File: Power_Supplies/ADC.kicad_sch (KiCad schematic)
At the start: 0 parts

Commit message: Added ADC schematic
yes
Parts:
- added C36, C38, C40: 0.1uF, Capacitor_SMD:C_0805_2012Metric, symbol Device:C
- added C37, C39, C41: 10uF, Capacitor_SMD:CP_Elec_4x5.8, symbol Device:C_Polarized_US
- added C42, C43: 1uF, Capacitor_SMD:CP_Elec_4x5.8, symbol Device:C_Polarized_US
- added IC1: PCM1808PWRG4, SamacSys_Parts:SOP65P640X120-14N, symbol SamacSys_Parts:PCM1808PWRG4
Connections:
- new net: C43.1, IC1.13 (VINL)
- new net: C42.1, IC1.14 (VINR)
- new net: C40.1, C41.1, IC1.1 (VREF)
- new net 3.3V: C38.2, C39.1, IC1.4 (VDD)
- new net 5V: C36.1, C37.1, IC1.3 (VCC)
- new net AGND: C36.2, C37.2, C38.1, C39.2, C40.2, C41.2, IC1.2 (AGND), IC1.5 (DGND)
- new net A_L_1: C43.2
- new net A_R_1: C42.2
- new net DATA_BIT_CLOCK: IC1.8 (BCK)
- new net D_OUT_1: IC1.9 (DOUT)
- new net FORMAT_SELECT: IC1.12 (FMT)
- new net LRCK: IC1.7 (LRCK)
- new net MCLK: IC1.6 (SCKI)
- new net MODE_0: IC1.10 (MD0)
- new net MODE_1: IC1.11 (MD1)

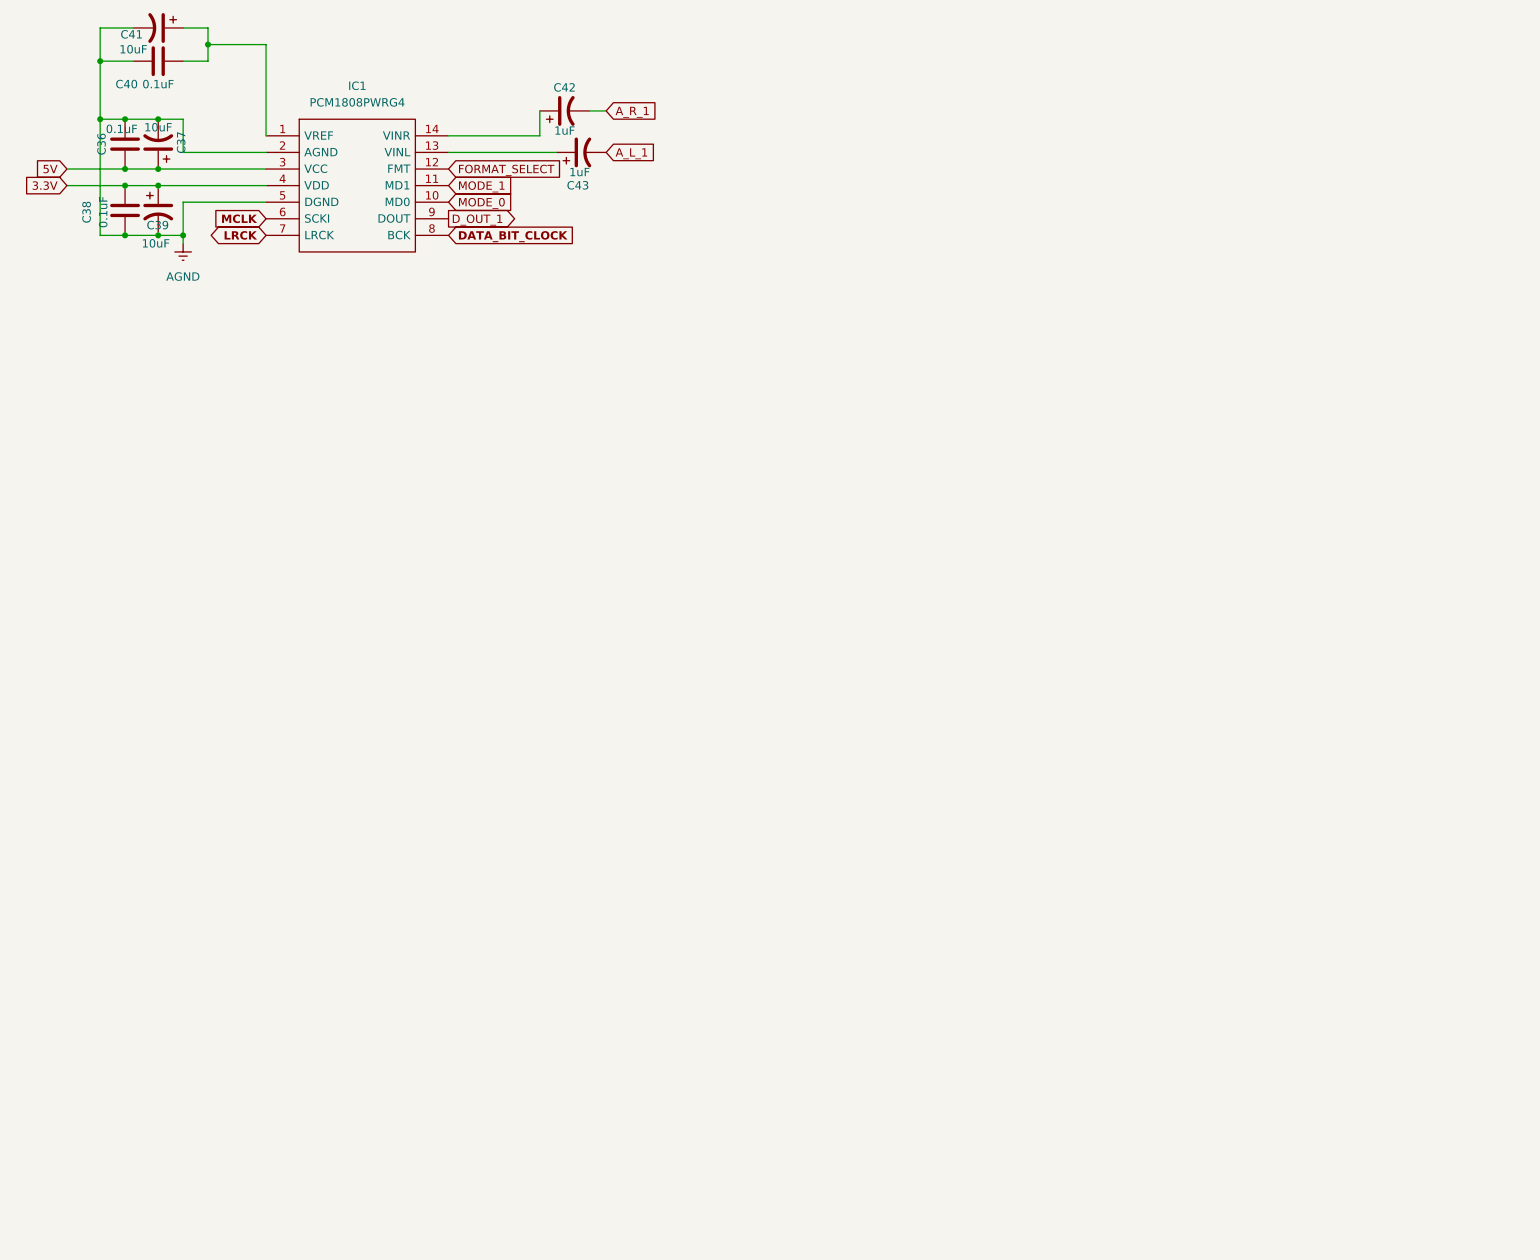
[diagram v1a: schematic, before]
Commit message: Added Phantom Power, updated Xcore library things
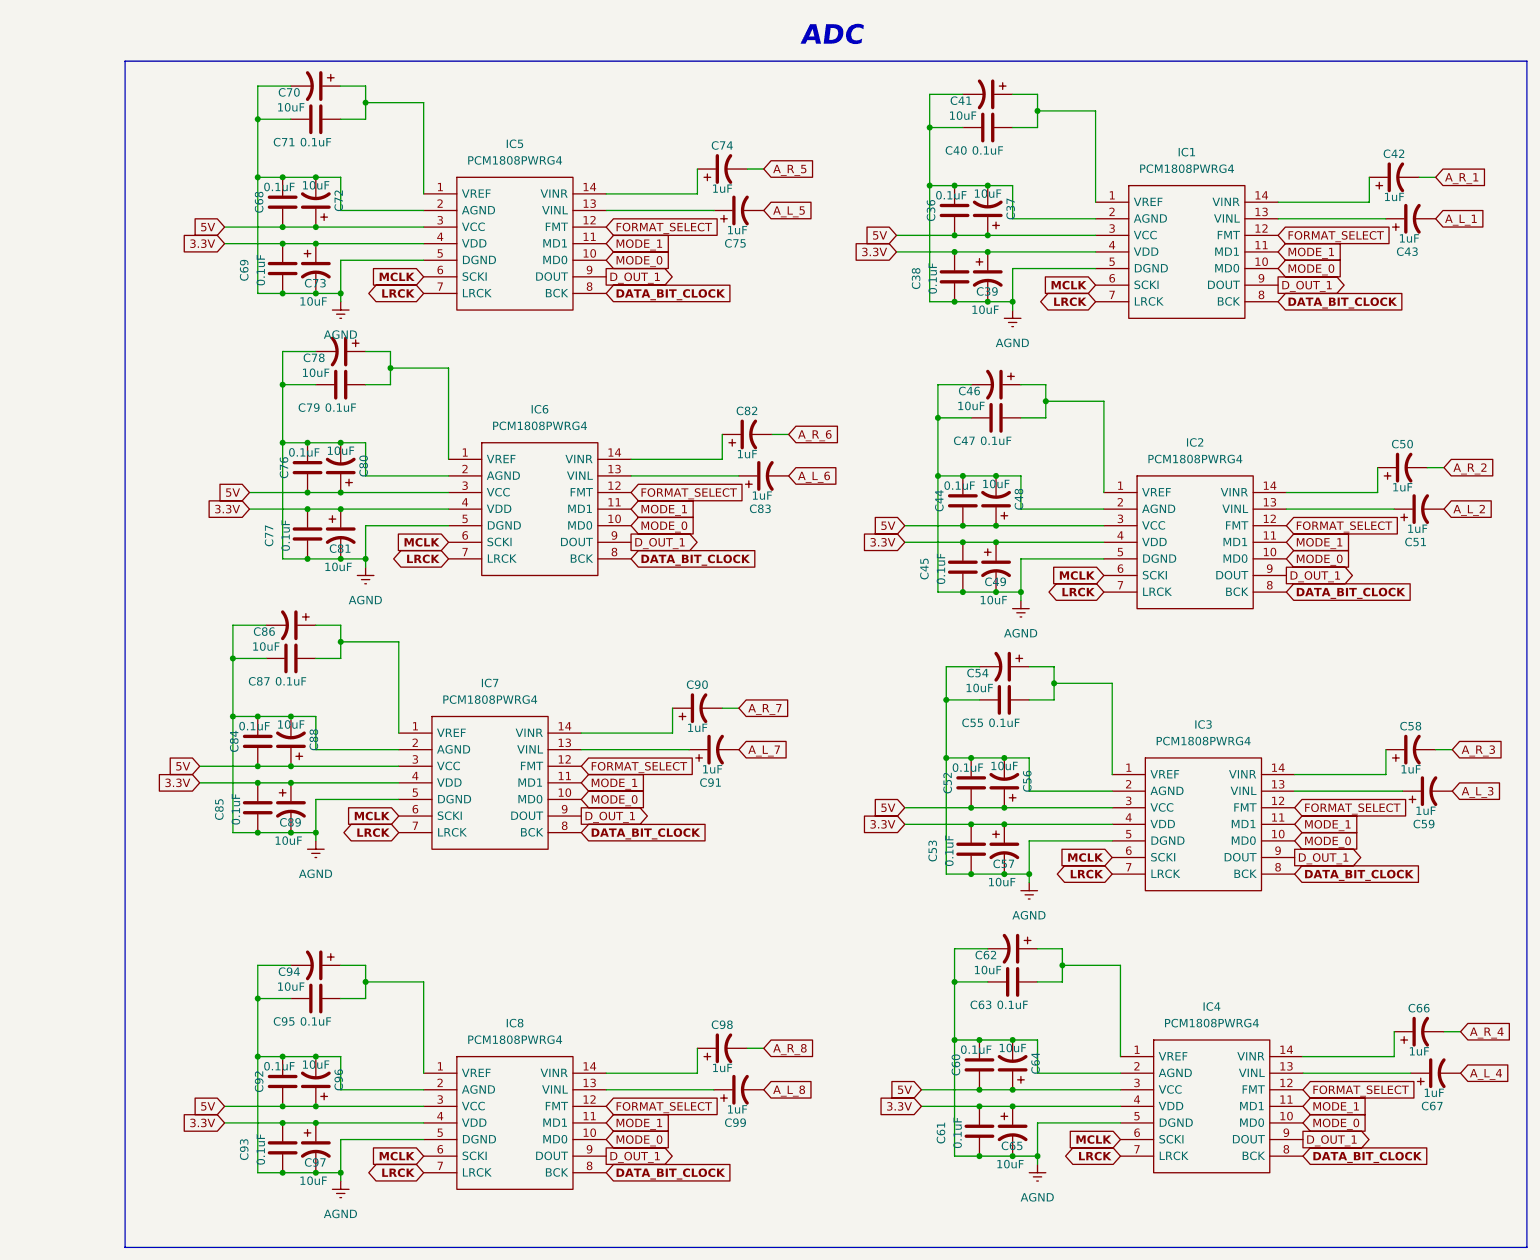
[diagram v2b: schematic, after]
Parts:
- added C44, C45, C47, C52, C53, C55, C60, C61, C63, C68, C69, C71, C76, C77, C79, C84, C85, C87, C92, C93, C95: 0.1uF, Capacitor_SMD:C_0805_2012Metric, symbol Device:C
- added C46, C48, C49, C54, C56, C57, C62, C64, C65, C70, C72, C73, C78, C80, C81, C86, C88, C89, C94, C96, C97: 10uF, Capacitor_SMD:CP_Elec_4x5.8, symbol Device:C_Polarized_US
- added C50, C51, C58, C59, C66, C67, C74, C75, C82, C83, C90, C91, C98, C99: 1uF, Capacitor_SMD:CP_Elec_4x5.8, symbol Device:C_Polarized_US
- added IC2, IC3, IC4, IC5, IC6, IC7, IC8: PCM1808PWRG4, SamacSys_Parts:SOP65P640X120-14N, symbol SamacSys_Parts:PCM1808PWRG4
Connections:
- net 3.3V: now also C45.2, C49.1, C53.2, C57.1, C61.2, C65.1, C69.2, C73.1, C77.2, C81.1, C85.2, C89.1, C93.2, C97.1, IC2.4 (VDD), IC3.4 (VDD), IC4.4 (VDD), IC5.4 (VDD), IC6.4 (VDD), IC7.4 (VDD), IC8.4 (VDD)
- net 5V: now also C44.1, C48.1, C52.1, C56.1, C60.1, C64.1, C68.1, C72.1, C76.1, C80.1, C84.1, C88.1, C92.1, C96.1, IC2.3 (VCC), IC3.3 (VCC), IC4.3 (VCC), IC5.3 (VCC), IC6.3 (VCC), IC7.3 (VCC), IC8.3 (VCC)
- net AGND: now also C44.2, C45.1, C46.2, C47.2, C48.2, C49.2, C52.2, C53.1, C54.2, C55.2, C56.2, C57.2, C60.2, C61.1, C62.2, C63.2, C64.2, C65.2, C68.2, C69.1, C70.2, C71.2, C72.2, C73.2, C76.2, C77.1, C78.2, C79.2, C80.2, C81.2, C84.2, C85.1, C86.2, C87.2, C88.2, C89.2, C92.2, C93.1, C94.2, C95.2, C96.2, C97.2, IC2.2 (AGND), IC2.5 (DGND), IC3.2 (AGND), IC3.5 (DGND), IC4.2 (AGND), IC4.5 (DGND), IC5.2 (AGND), IC5.5 (DGND), IC6.2 (AGND), IC6.5 (DGND), IC7.2 (AGND), IC7.5 (DGND), IC8.2 (AGND), IC8.5 (DGND)
- net DATA_BIT_CLOCK: now also IC2.8 (BCK), IC3.8 (BCK), IC4.8 (BCK), IC5.8 (BCK), IC6.8 (BCK), IC7.8 (BCK), IC8.8 (BCK)
- net D_OUT_1: now also IC2.9 (DOUT), IC3.9 (DOUT), IC4.9 (DOUT), IC5.9 (DOUT), IC6.9 (DOUT), IC7.9 (DOUT), IC8.9 (DOUT)
- net FORMAT_SELECT: now also IC2.12 (FMT), IC3.12 (FMT), IC4.12 (FMT), IC5.12 (FMT), IC6.12 (FMT), IC7.12 (FMT), IC8.12 (FMT)
- net LRCK: now also IC2.7 (LRCK), IC3.7 (LRCK), IC4.7 (LRCK), IC5.7 (LRCK), IC6.7 (LRCK), IC7.7 (LRCK), IC8.7 (LRCK)
- net MCLK: now also IC2.6 (SCKI), IC3.6 (SCKI), IC4.6 (SCKI), IC5.6 (SCKI), IC6.6 (SCKI), IC7.6 (SCKI), IC8.6 (SCKI)
- net MODE_0: now also IC2.10 (MD0), IC3.10 (MD0), IC4.10 (MD0), IC5.10 (MD0), IC6.10 (MD0), IC7.10 (MD0), IC8.10 (MD0)
- net MODE_1: now also IC2.11 (MD1), IC3.11 (MD1), IC4.11 (MD1), IC5.11 (MD1), IC6.11 (MD1), IC7.11 (MD1), IC8.11 (MD1)
- new net: C94.1, C95.1, IC8.1 (VREF)
- new net: C98.1, IC8.14 (VINR)
- new net: C51.1, IC2.13 (VINL)
- new net: C74.1, IC5.14 (VINR)
- new net: C78.1, C79.1, IC6.1 (VREF)
- new net: C83.1, IC6.13 (VINL)
- new net: C82.1, IC6.14 (VINR)
- new net: C58.1, IC3.14 (VINR)
- new net: C62.1, C63.1, IC4.1 (VREF)
- new net: C67.1, IC4.13 (VINL)
- new net: C66.1, IC4.14 (VINR)
- new net: C54.1, C55.1, IC3.1 (VREF)
- new net: C59.1, IC3.13 (VINL)
- new net: C46.1, C47.1, IC2.1 (VREF)
- new net: C86.1, C87.1, IC7.1 (VREF)
- new net: C91.1, IC7.13 (VINL)
- new net: C90.1, IC7.14 (VINR)
- new net: C50.1, IC2.14 (VINR)
- new net: C70.1, C71.1, IC5.1 (VREF)
- new net: C75.1, IC5.13 (VINL)
- new net: C99.1, IC8.13 (VINL)
- new net A_L_2: C51.2
- new net A_L_3: C59.2
- new net A_L_4: C67.2
- new net A_L_5: C75.2
- new net A_L_6: C83.2
- new net A_L_7: C91.2
- new net A_L_8: C99.2
- new net A_R_2: C50.2
- new net A_R_3: C58.2
- new net A_R_4: C66.2
- new net A_R_5: C74.2
- new net A_R_6: C82.2
- new net A_R_7: C90.2
- new net A_R_8: C98.2
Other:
- note added: "ADC"
- moved on the sheet: C36, C37, C38, C39, C40, C41, C42, C43, IC1

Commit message: Add files via upload
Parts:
- removed C36, C63, C76, C77, C79, C84, C85, C87, C92, C93, C95: 0.1uF, Capacitor_SMD:C_0805_2012Metric, symbol Device:C
- removed C37, C46, C48, C49, C54, C56, C57, C62, C64, C65, C78, C80, C81, C86, C88, C89, C94, C96, C97: 10uF, Capacitor_SMD:CP_Elec_4x5.8, symbol Device:C_Polarized_US
- removed C42, C43, C51, C58, C59, C66, C67, C82, C83, C90, C91, C98, C99: 1uF, Capacitor_SMD:CP_Elec_4x5.8, symbol Device:C_Polarized_US
- removed IC1, IC2, IC3, IC4, IC6, IC7, IC8: PCM1808PWRG4, SamacSys_Parts:SOP65P640X120-14N, symbol SamacSys_Parts:PCM1808PWRG4
- added C36: 10uF, Capacitor_SMD:CP_Elec_4x5.8, symbol Device:C_Polarized_US
- added C37, C51: 0.1uF, Capacitor_SMD:C_0805_2012Metric, symbol Device:C
- added C42, C49: 150p, Capacitor_SMD:C_0402_1005Metric, symbol Device:C
- added C43, C48: 100n, Capacitor_SMD:C_0402_1005Metric, symbol Device:C
- added C46: 1n, Capacitor_SMD:C_0402_1005Metric, symbol Device:C
- added C54, C56: 100pF, Capacitor_SMD:C_0805_2012Metric, symbol Device:C
- added C57: 1uF, Capacitor_SMD:C_0805_2012Metric, symbol Device:C
- added C58: 10uF, Capacitor_SMD:C_0805_2012Metric, symbol Device:C
- added C59: 2.2uF, Capacitor_SMD:C_0805_2012Metric, symbol Device:C
- added D3: PESD3V3L1BA,115, Diode_SMD:D_SOD-323, symbol Device:D_TVS
- added IC1: PCM4201PWR, SOP65P640X120-16N, symbol SamacSys_Parts:PCM4201PWR
- added J3: 031-5640-1010, PhilsLab_Footprints_KiCad6:AMPHENOL-BNC-031-5640-1010, symbol Connector:Conn_Coaxial
- added J5: AudioJack2, symbol Connector_Audio:AudioJack2
- added R57, R64, R65: 1k, Resistor_SMD:R_0402_1005Metric, symbol Device:R
- added R58, R59: 2M2, Resistor_SMD:R_0402_1005Metric, symbol Device:R
- added R61: 6k8, Resistor_SMD:R_0402_1005Metric, symbol Device:R
- added R62: 22k, Resistor_SMD:R_0402_1005Metric, symbol Device:R
- added R63: 12k, Resistor_SMD:R_0402_1005Metric, symbol Device:R
- added R66, R67: 10k, Resistor_SMD:R_0805_2012Metric, symbol Device:R
- added R68, R69: 2.49k, Resistor_SMD:R_0805_2012Metric, symbol Device:R
- added R70, R71: 40.2, Resistor_SMD:R_0805_2012Metric, symbol Device:R
- added R72: 270, Resistor_SMD:R_0805_2012Metric, symbol Device:R
- added R73: 1k, Resistor_SMD:R_0805_2012Metric, symbol Device:R
- added R74: 249k, Resistor_SMD:R_0603_1608Metric, symbol Device:R
- added R75: 499k, Resistor_SMD:R_0603_1608Metric, symbol Device:R
- added U14, U15: MCP6001T-E/OT, Package_TO_SOT_SMD:SOT-23-5, symbol Amplifier_Operational:MCP6001-OT
- added U16: OPA2134, symbol Amplifier_Operational:OPA2134
- added U17: LM27761, Package_SON:WSON-8-1EP_2x2mm_P0.5mm_EP0.9x1.6mm, symbol Regulator_SwitchedCapacitor:LM27761
- C44: value 0.1uF -> 100n; footprint Capacitor_SMD:C_0805_2012Metric -> Capacitor_SMD:C_0402_1005Metric
- C45: value 0.1uF -> 1n; footprint Capacitor_SMD:C_0805_2012Metric -> Capacitor_SMD:C_0402_1005Metric
- C47: value 0.1uF -> 150p; footprint Capacitor_SMD:C_0805_2012Metric -> Capacitor_SMD:C_0402_1005Metric
- C50: value 1uF -> 10uF
- C52: value 0.1uF -> 1nF; footprint Capacitor_SMD:C_0805_2012Metric -> Capacitor_SMD:C_0402_1005Metric
- C53: value 0.1uF -> 100uF
- C55: value 0.1uF -> 0.022uF
- C60: value 0.1uF -> 4.7uF
- C61: value 0.1uF -> 1uF
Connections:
- net 3.3V: now also C39.2, C44.1, C48.1, IC1.13 (VDD), U14.5 (V+), U15.5 (V+); no longer C39.1, C45.2, C53.2, C61.2
- net 5V: now also C61.2, C58.2, R66.1, U16.8 (V+), U17.1 (VIN), U17.6 (EN); no longer C44.1, C52.1, C60.1
- net AGND: now also C40.1, C36.2, C37.2, IC1.15 (VREF-), IC1.3 (AGND), J5.S; no longer C38.1, C39.2, C40.2, C44.2, C45.1, C47.2, C52.2, C53.1, C55.2, C60.2, C61.1
- net DATA_BIT_CLOCK: now also IC1.11 (BCK)
- net D_OUT_1: now also IC1.9 (DATA)
- net MCLK: now also IC1.12 (SCKI)
- net ADC1_IN+: now reaches C55.1
- net ADC1_IN+: now also C54.2, R70.2
- net 5V_LDO: now reaches C41.1
- net 5V_LDO: now also C40.2, IC1.4 (VCC); no longer C40.1
- net IN_AA_BUF_IN: now reaches C47.1
- net IN_AA_BUF_IN: now also R63.1, U15.3 (+)
- net at C50.1: now also C51.2, R66.2, R67.1, U16.3 (+), U16.5 (+)
- net A_R_2 renamed DGND
- net DGND: now also C38.1, C39.1, C44.2, C60.1, C61.1, C48.2, C51.1, C54.1, C56.2, C58.1, C59.1, IC1.14 (DGND), R67.2, R75.2, U17.2 (GND), U17.9 (PAD)
- new net: C52.1, R68.1, R71.1, R72.2, U16.1
- new net: C52.2, R72.1, R73.2, U16.2 (-)
- new net: C46.1, R62.1, R63.2
- new net: C45.1, R61.1, R62.2
- new net: R68.2, R69.1, U16.6 (-)
- new net: C53.1, R73.1
- new net: C53.2, J5.T
- new net: R69.2, R70.1, U16.7
- new net: C36.1, C37.1, IC1.16 (VREF+)
- new net: R74.2, R75.1, U17.5 (VFB)
- new net: C60.2, U17.3 (CPOUT)
- new net: C57.1, U17.7 (C-)
- new net: C57.2, U17.8 (C+)
- new net -5V: C59.2, R74.1, U17.4 (VOUT)
- new net ADC1_IN-: C55.2, C56.1, R71.2
- new net ADC_IN+: C49.1, R64.1
- new net ADC_IN-: C49.2, R65.1
- new net GND: C42.2, C45.2, C47.2, D3.2 (A2), J3.2 (Ext), R58.1, U14.2 (V-), U15.2 (V-)
- new net IN: D3.1 (A1), J3.1 (In), R57.2
- new net IN_AA_BUF_OUT: C46.2, R64.2, U15.1, U15.4 (-)
- new net IN_BUF: C43.1, R59.1, U14.3 (+)
- new net IN_BUF_OUT: R61.2, U14.1, U14.4 (-)
- new net IN_RF: C42.1, C43.2, R57.1, R58.2
- new net VCOM: R59.2, R65.2
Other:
- note added: "3rd order Butterworth anti-aliasing (low-pass filter) fc=25kHz"
- note added: "BNC connector"
- note added: "Both ADC inputs should be at same VCOM"
- note added: "HP filter: fc=1.4Hz"
- note added: "Input voltage must be in -1.65V to +1.65V range!"
- note added: "MCP6001: I/O Rail-to-Rail, Single-Supply (1V8 to 5V), high-impedance input CMOS, low bias currents, unity gain stable"
- note added: "RF filter: fc=1.1MHz"
- note added: "Rin = 1.1M"
- note added: "Single-ended to 'balanced' conversion"
- moved on the sheet: C68, C69, C70, C71, C72, C73, C74, C75, IC5
